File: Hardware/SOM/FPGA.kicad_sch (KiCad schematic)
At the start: 40 parts, among them U1 LFE5UM5G-85F

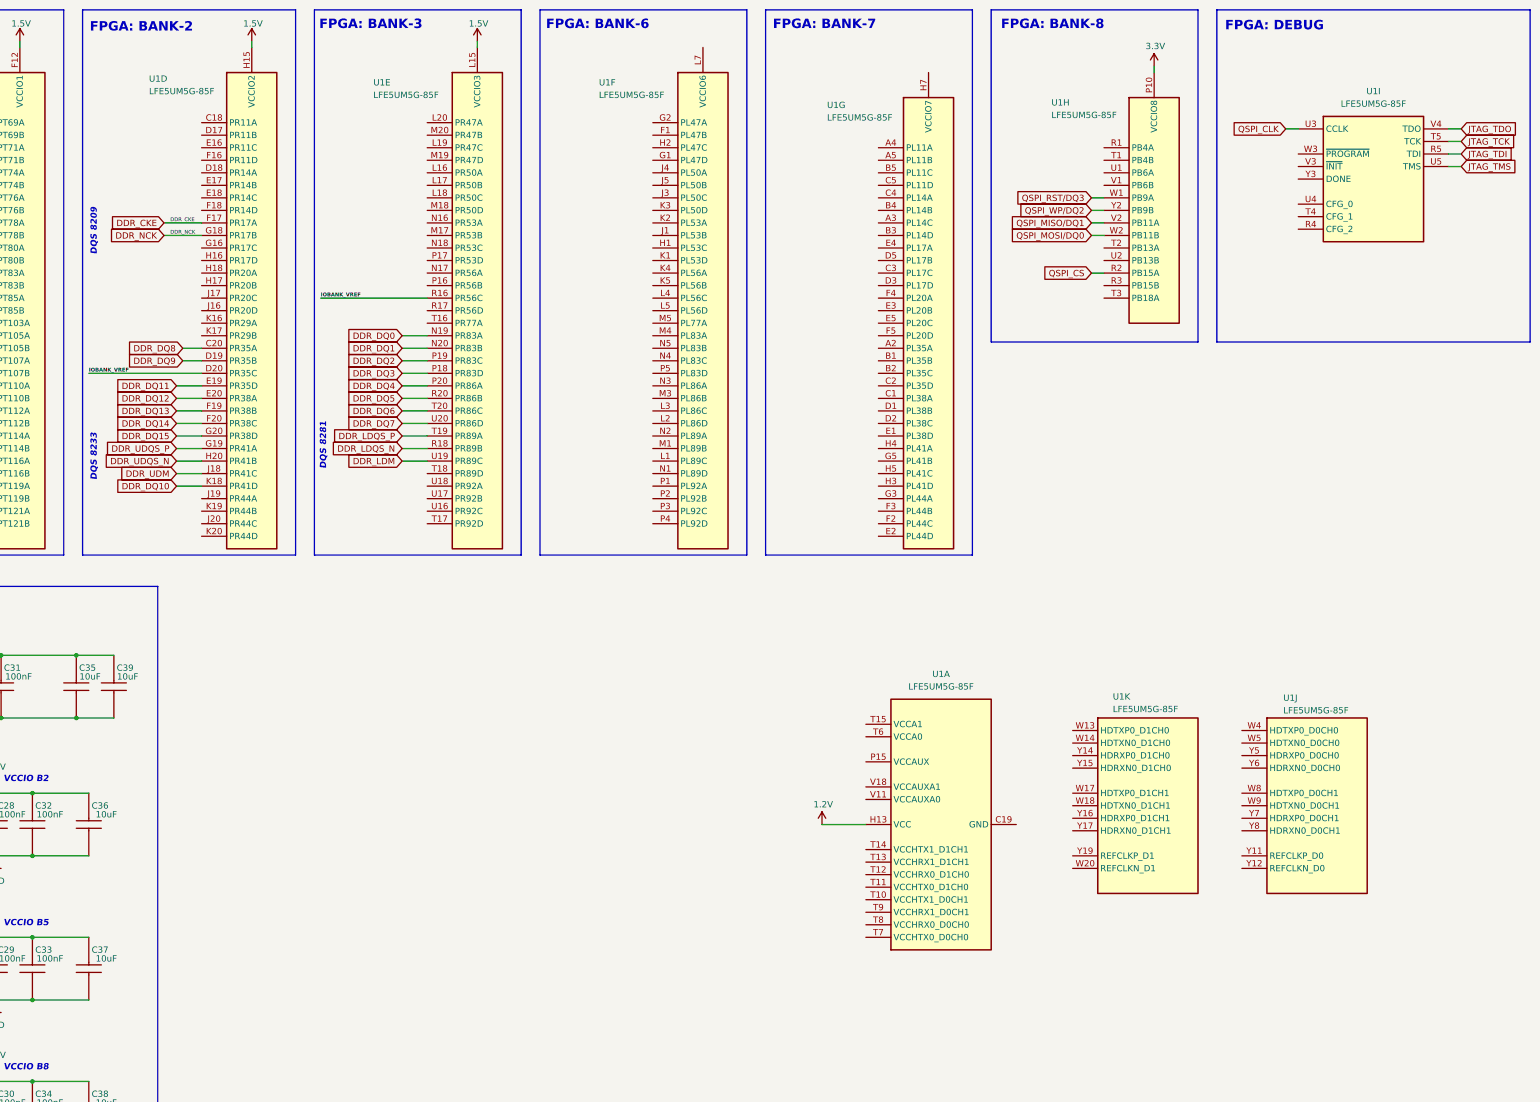
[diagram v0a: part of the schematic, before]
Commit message: SOM: Boot mode CFG
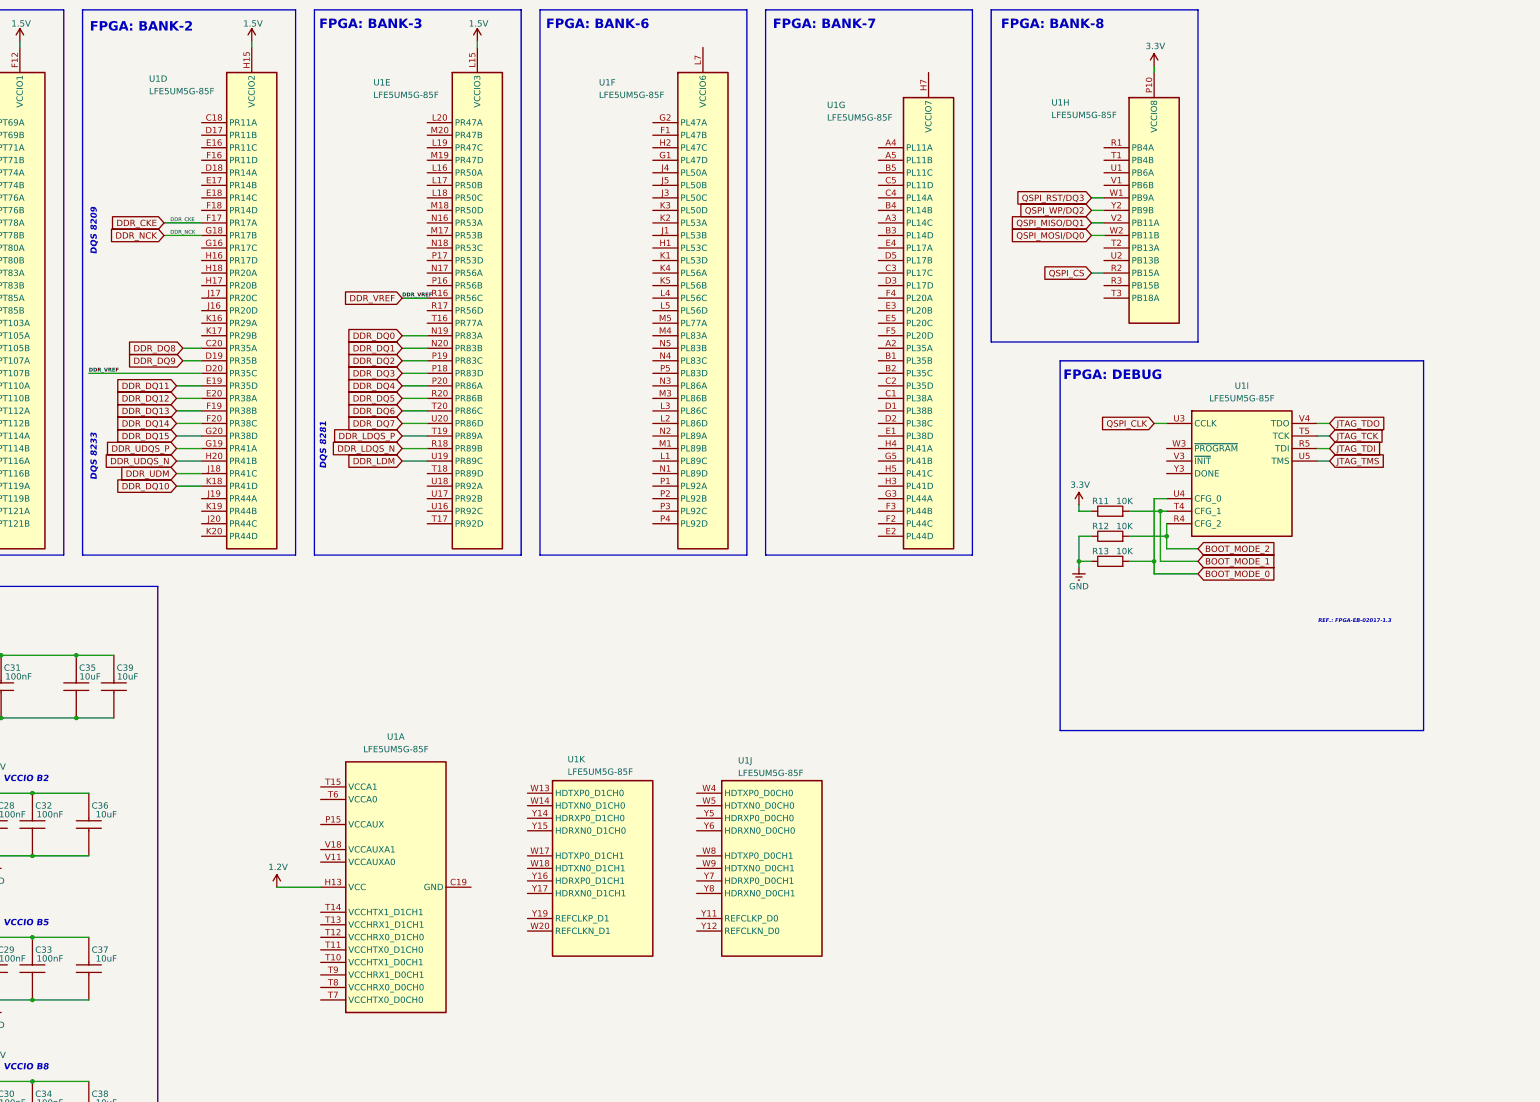
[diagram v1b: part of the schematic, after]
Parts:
- added R11, R12, R13: 10K, Resistor_SMD:R_0402_1005Metric, symbol Device:R
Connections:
- net 3.3V: now also R11.1
- net GND: now also R12.1, R13.1
- net BOOT_MODE_2: now reaches U1.R4 (CFG_2)
- net BOOT_MODE_2: now also R12.2
- net BOOT_MODE_1: now reaches U1.T4 (CFG_1)
- net BOOT_MODE_1: now also R11.2
- net BOOT_MODE_0: now reaches U1.U4 (CFG_0)
- net BOOT_MODE_0: now also R13.2
- net IOBANK_VREF renamed DDR_VREF
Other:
- note added: "REF.: FPGA-EB-02017-1.3"
- moved on the sheet: U1A, U1I, U1J, U1K

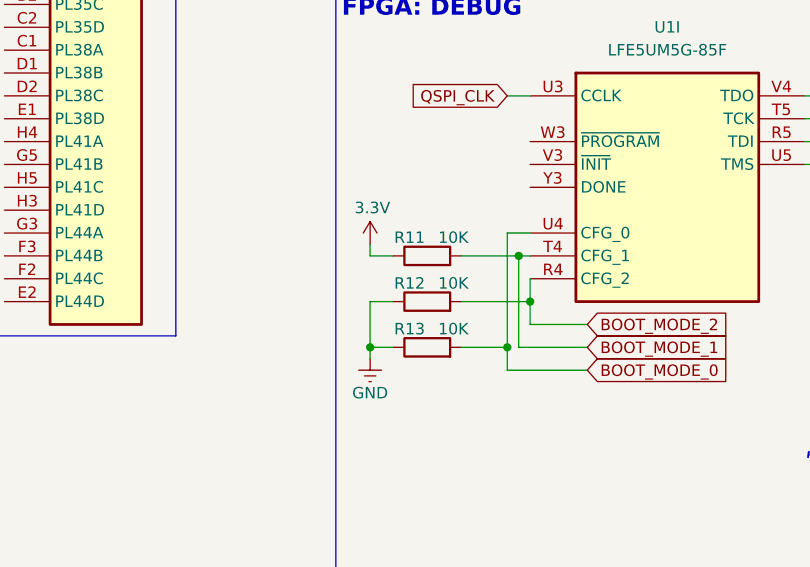
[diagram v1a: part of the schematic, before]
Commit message: SOM: DDR pull-ups
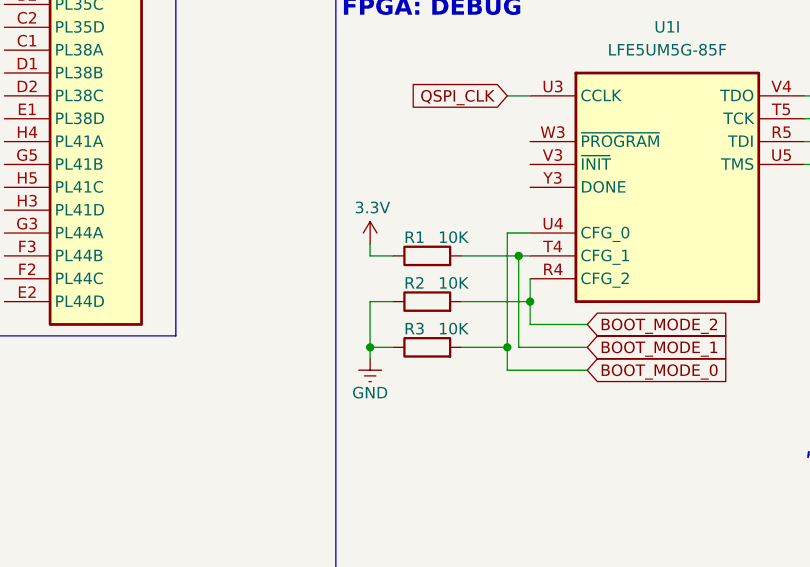
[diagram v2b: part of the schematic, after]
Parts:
- renumbered R11 to R1, R12 to R2, R13 to R3
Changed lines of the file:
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@@
 		(on_board yes)
 		(dnp no)
-		(property "Reference" "R13"
+		(property "Reference" "R3"
 			(at 318.516 130.048 90)
 			(effects
@@
 			(project "LFE5UM5G-85F_SOM"
 				(path "/de32abb0-ff3b-4c67-a91a-eed08140b1b2/c389ef9b-5ef6-4b55-8e02-1ff1b5373fc6"
-					(reference "R13")
+					(reference "R3")
 					(unit 1)
 				)
@@
 		(on_board yes)
 		(dnp no)
-		(property "Reference" "#PWR018"
+		(property "Reference" "#PWR019"
 			(at 190.5 30.48 0)
 			(effects
@@
 			(project "LFE5UM5G-85F_SOM"
 				(path "/de32abb0-ff3b-4c67-a91a-eed08140b1b2/c389ef9b-5ef6-4b55-8e02-1ff1b5373fc6"
-					(reference "#PWR018")
+					(reference "#PWR019")
 					(unit 1)
 				)
@@
 		(on_board yes)
 		(dnp no)
-		(property "Reference" "R11"
+		(property "Reference" "R1"
 			(at 318.516 119.888 90)
 			(effects
@@
 			(project "LFE5UM5G-85F_SOM"
 				(path "/de32abb0-ff3b-4c67-a91a-eed08140b1b2/c389ef9b-5ef6-4b55-8e02-1ff1b5373fc6"
-					(reference "R11")
+					(reference "R1")
 					(unit 1)
 				)
@@
 		(on_board yes)
 		(dnp no)
-		(property "Reference" "#PWR037"
+		(property "Reference" "#PWR021"
 			(at 312.42 139.7 0)
 			(effects
@@
 			(project "LFE5UM5G-85F_SOM"
 				(path "/de32abb0-ff3b-4c67-a91a-eed08140b1b2/c389ef9b-5ef6-4b55-8e02-1ff1b5373fc6"
-					(reference "#PWR037")
+					(reference "#PWR021")
 					(unit 1)
 				)
@@
 		(on_board yes)
 		(dnp no)
-		(property "Reference" "#PWR020"
+		(property "Reference" "#PWR022"
 			(at 327.66 35.56 0)
 			(effects
@@
 			(project "LFE5UM5G-85F_SOM"
 				(path "/de32abb0-ff3b-4c67-a91a-eed08140b1b2/c389ef9b-5ef6-4b55-8e02-1ff1b5373fc6"
-					(reference "#PWR020")
+					(reference "#PWR022")
 					(unit 1)
 				)
@@
 		(on_board yes)
 		(dnp no)
-		(property "Reference" "#PWR019"
+		(property "Reference" "#PWR018"
 			(at 149.86 201.93 0)
 			(effects
@@
 			(project "LFE5UM5G-85F_SOM"
 				(path "/de32abb0-ff3b-4c67-a91a-eed08140b1b2/c389ef9b-5ef6-4b55-8e02-1ff1b5373fc6"
-					(reference "#PWR019")
+					(reference "#PWR018")
 					(unit 1)
 				)
@@
 		(on_board yes)
 		(dnp no)
-		(property "Reference" "#PWR038"
+		(property "Reference" "#PWR020"
 			(at 312.42 124.46 0)
 			(effects
@@
 			(project "LFE5UM5G-85F_SOM"
 				(path "/de32abb0-ff3b-4c67-a91a-eed08140b1b2/c389ef9b-5ef6-4b55-8e02-1ff1b5373fc6"
-					(reference "#PWR038")
+					(reference "#PWR020")
 					(unit 1)
 				)
@@
 		(on_board yes)
 		(dnp no)
-		(property "Reference" "R12"
+		(property "Reference" "R2"
 			(at 318.516 124.968 90)
 			(effects
@@
 			(project "LFE5UM5G-85F_SOM"
 				(path "/de32abb0-ff3b-4c67-a91a-eed08140b1b2/c389ef9b-5ef6-4b55-8e02-1ff1b5373fc6"
-					(reference "R12")
+					(reference "R2")
 					(unit 1)
 				)

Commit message: DDR Banks Vref
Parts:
- removed R1, R2, R3: 10K, Resistor_SMD:R_0402_1005Metric, symbol Device:R
- removed unit 9 of U1
- added C59, C61, C63: 1uF, Capacitor_SMD:C_0402_1005Metric, symbol RA8M1:885012205092
- added C60, C62, C64: 100nF, Capacitor_SMD:C_0402_1005Metric, symbol RA8M1:885012205092
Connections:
- net 1.5V: now also C12.2, C4.2, C8.2, U1.L6 (VCCIO6), U1.L7 (VCCIO6), U1.M6 (VCCIO6); no longer C15.2, C19.2, C24.2
- net DDR_A0: now also U1.L5 (PL56D); no longer U1.E14 (PT85B)
- net DDR_A1: now also U1.M5 (PL77A); no longer U1.A15 (PT103A)
- net DDR_A10: now also U1.N2 (PL89A); no longer U1.B17 (PT114A)
- net DDR_A11: now also U1.M1 (PL89B); no longer U1.C17 (PT114B)
- net DDR_A12: now also U1.L1 (PL89C); no longer U1.A17 (PT116A)
- net DDR_A13: now also U1.N1 (PL89D); no longer U1.B18 (PT116B)
- net DDR_A14: now also U1.P1 (PL92A); no longer U1.A18 (PT119A)
- net DDR_A2: now also U1.M4 (PL83A); no longer U1.B15 (PT105A)
- net DDR_A3: now also U1.N5 (PL83B); no longer U1.C15 (PT105B)
- net DDR_A4: now also U1.N4 (PL83C); no longer U1.D15 (PT107A)
- net DDR_A5: now also U1.P5 (PL83D); no longer U1.E15 (PT107B)
- net DDR_A6: now also U1.N3 (PL86A); no longer U1.A16 (PT110A)
- net DDR_A7: now also U1.M3 (PL86B); no longer U1.B16 (PT110B)
- net DDR_A8: now also U1.L3 (PL86C); no longer U1.C16 (PT112A)
- net DDR_A9: now also U1.L2 (PL86D); no longer U1.D16 (PT112B)
- net DDR_BA0: now also U1.P2 (PL92B); no longer U1.B19 (PT119B)
- net DDR_BA1: now also U1.P3 (PL92C); no longer U1.A19 (PT121A)
- net DDR_BA2: now also U1.P4 (PL92D); no longer U1.B20 (PT121B)
- net DDR_CAS: now also U1.K1 (PL53D); no longer U1.A14 (PT83A)
- net DDR_CK: now also U1.K3 (PL50D); no longer U1.B13 (PT78A)
- net DDR_CS: now also U1.J1 (PL53B); no longer U1.D13 (PT80A)
- net DDR_ODT: now also U1.L4 (PL56C); no longer U1.D14 (PT85A)
- net DDR_RAS: now also U1.H1 (PL53C); no longer U1.E13 (PT80B)
- net DDR_RST: now also U1.K2 (PL53A); no longer U1.C13 (PT78B)
- net DDR_VREF: now also U1.K5 (PL56B), U1.P16 (PR56B), C59.2, C60.2, C61.2, C62.2, C63.2, C64.2; no longer U1.R16 (PR56C)
- net DDR_WE: now also U1.K4 (PL56A); no longer U1.C14 (PT83B)
- net GND: now also C59.1, C60.1, C61.1, C62.1, C63.1, C64.1
- new net: C15.2, C19.2, C24.2
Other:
- note added: "DDR VREF pins"
- note removed: "FPGA: DEBUG"
- note removed: "REF.: FPGA-EB-02017-1.3"
- moved on the sheet: U1A, U1J, U1K

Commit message: SOM: power supplies
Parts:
- added C65, C66: 10uF, Capacitor_SMD:C_0402_1005Metric, symbol RA8M1:885012205092
- added C67, C68, C69, C70, C71, C72, C73, C74: 100nF, Capacitor_SMD:C_0402_1005Metric, symbol RA8M1:885012205092
- added FB1: FerriteBead, Inductor_SMD:L_1206_3216Metric, symbol Device:FerriteBead
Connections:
- net GND: now also U1.B14 (GND), U1.B7 (GND), U1.C19 (GND), U1.D4 (GND), U1.F13 (GND), U1.F14 (GND), U1.F7 (GND), U1.F8 (GND), U1.G10 (GND), U1.G11 (GND), U1.G12 (GND), U1.G13 (GND), U1.G14 (GND), U1.G15 (GND), U1.G17 (GND), U1.G4 (GND), U1.G6 (GND), U1.G7 (GND), U1.G8 (GND), U1.G9 (GND), U1.H19 (GND), U1.J10 (GND), U1.J11 (GND), U1.J12 (GND), U1.J14 (GND), U1.J2 (GND), U1.J7 (GND), U1.J9 (GND), U1.K10 (GND), U1.K11 (GND), U1.K12 (GND), U1.K14 (GND), U1.K15 (GND), U1.K6 (GND), U1.K7 (GND), U1.K9 (GND), U1.L10 (GND), U1.L11 (GND), U1.L12 (GND), U1.L9 (GND), U1.M10 (GND), U1.M11 (GND), U1.M12 (GND), U1.M14 (GND), U1.M16 (GND), U1.M2 (GND), U1.M7 (GND), U1.M9 (GND), U1.N14 (GND), U1.N15 (GND), U1.N6 (GND), U1.N7 (GND), U1.P11 (GND), U1.P12 (GND), U1.P13 (GND), U1.P14 (GND), U1.P7 (GND), U1.P8 (GND), U1.R19 (GND), U1.U10 (GND), U1.U11 (GND), U1.U12 (GND), U1.U13 (GND), U1.U14 (GND), U1.U7 (GND), U1.U8 (GND), U1.U9 (GND), U1.V12 (GND), U1.V13 (GND), U1.V14 (GND), U1.V15 (GND), U1.V16 (GND), U1.V19 (GND), U1.V20 (GND), U1.V5 (GND), U1.V6 (GND), U1.V7 (GND), U1.V8 (GND), U1.V9 (GND), U1.W12 (GND), U1.W15 (GND), U1.W16 (GND), U1.W19 (GND), U1.W6 (GND), U1.W7 (GND), C65.1, C66.1, C67.1, C68.1, C69.1, C70.1, C71.1, C72.1, C73.1, C74.1
- net 2.5V_A: now reaches U1.F15 (VCCAUX), U1.F6 (VCCAUX), U1.P15 (VCCAUX), U1.P6 (VCCAUX)
- net 2.5V_A: now also U1.T15 (VCCA1), U1.T6 (VCCA0), U1.U15 (VCCA1), U1.U6 (VCCA0), U1.V10 (VCCAUXA0), U1.V11 (VCCAUXA0), U1.V17 (VCCAUXA1), U1.V18 (VCCAUXA1), C65.2, C66.2, C67.2, C68.2, C69.2, C70.2, C71.2, C72.2, C73.2, C74.2, FB1.2
- net at U1.T10 (VCCHTX1_D0CH1): now also U1.T14 (VCCHTX1_D1CH1)
- net at U1.T11 (VCCHTX0_D1CH0): now also U1.T7 (VCCHTX0_D0CH0)
- net at U1.T12 (VCCHRX0_D1CH0): now also U1.T8 (VCCHRX0_D0CH0)
- net at U1.T13 (VCCHRX1_D1CH1): now also U1.T9 (VCCHRX1_D0CH1)
- new net 2.5V: FB1.1
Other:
- note added: "DDR VREF PINS"
- note added: "FPGA Power"
- note removed: "FPGA Decoupling"
- moved on the sheet: C59, C60, C61, C62, C63, C64, U1A
